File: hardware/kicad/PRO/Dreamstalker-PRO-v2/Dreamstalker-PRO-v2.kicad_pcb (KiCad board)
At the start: 2 copper layers, 79 x 85 mm, 110 parts, among them J1 UART Header, J2 JTAG Header, J3 ST-033, J4 ATTEND_112J-TDAR-R01, J5 USB Power, J6 Li-Po 3.7V, M1 Vibration Motor, Q1 IRLML2402, Q2 BC807-40, Q3 BC807-40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

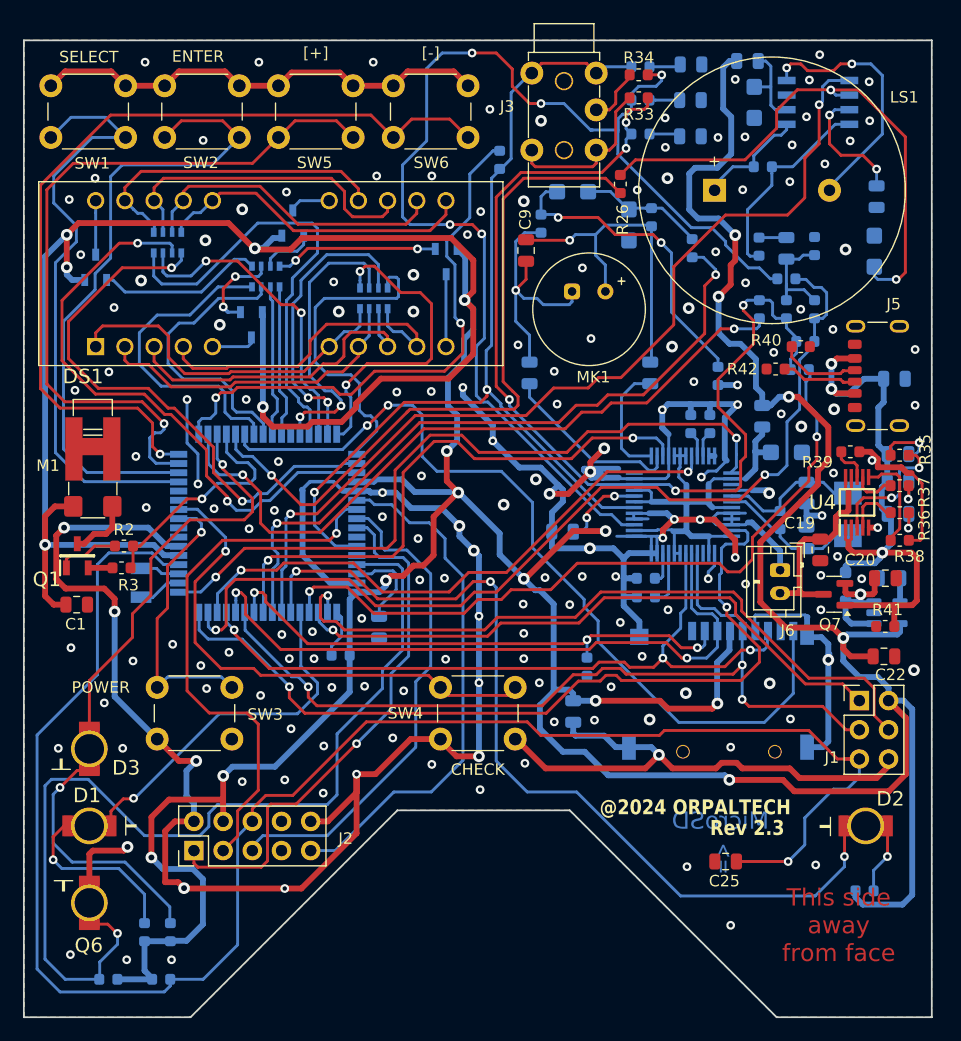
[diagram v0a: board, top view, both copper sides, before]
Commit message: 1) Fixed: battery monitor not able to detect low-battery state (Now get battery monitor signal from LDO input). 2) Other planned updates.
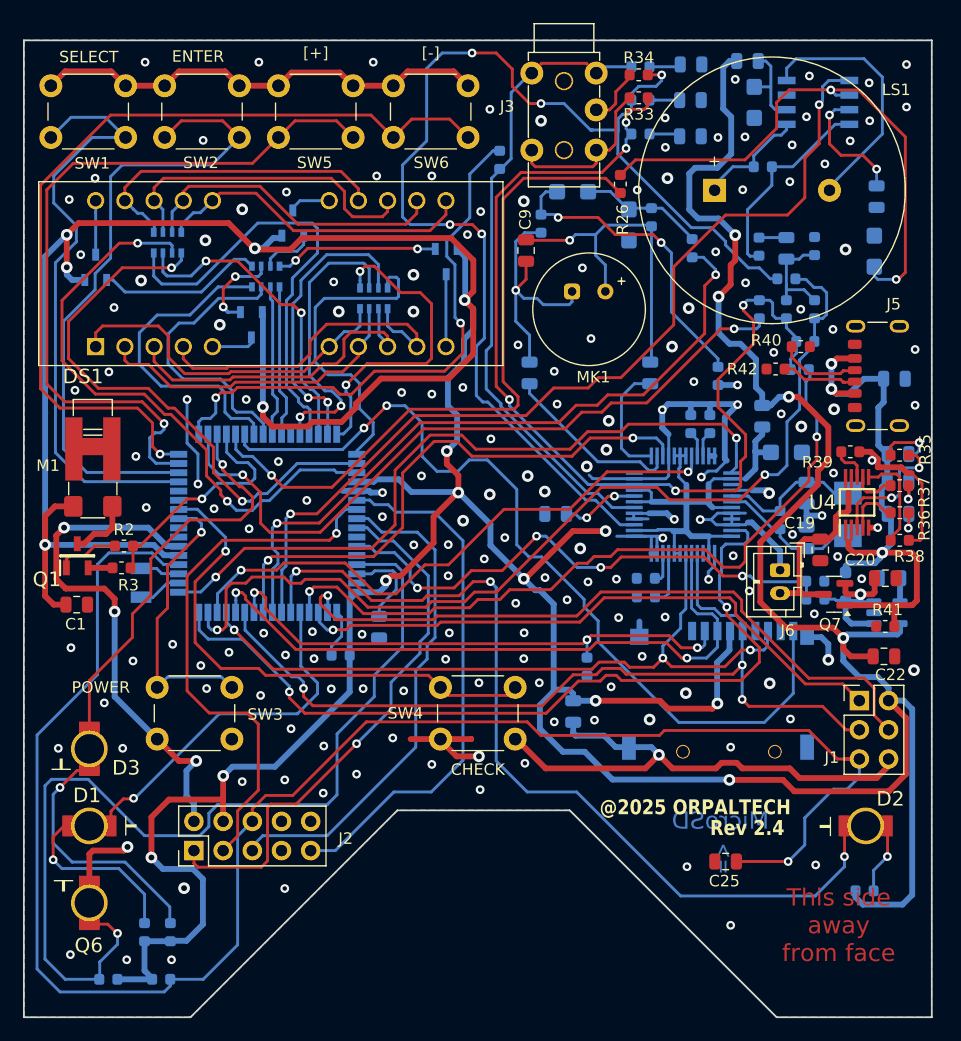
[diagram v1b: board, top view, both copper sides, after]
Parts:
- added R43: 30K, Dreamstalker-Footprints:R_0603_1608Metric, B.Cu at (158.4, 90.6)
- added R44: 15K, Dreamstalker-Footprints:R_0603_1608Metric, B.Cu at (158.4, 89.1)
- moved C13 1.65 mm to (135.8, 83.2)
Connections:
- U1 pad 59: /GBUF -> /BM
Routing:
- net GND: track 414.1 -> 250.1 mm, vias 174 -> 177
- net /BM: track 0.00 -> 47.1 mm, vias 0 -> 4
- net /GBUF: track 82.5 -> 56.1 mm, vias 2 -> 0
- net /VSVDD: track 43.2 -> 45.8 mm
- net /V_IN: track 12.0 -> 14.1 mm
- net /SILENT: track 61.8 -> 60.2 mm
- net /PDI: track 62.2 -> 60.8 mm
- net /XRESET: track 49.7 -> 48.5 mm
- net /XDCS: track 63.1 -> 62.1 mm
- net /TMS: track 42.9 -> 43.9 mm
- net /TCK: track 46.8 -> 47.7 mm
- net /TDI: track 45.5 -> 46.3 mm
- net /MOSI: track 57.7 -> 57.0 mm
- net /CD: track 74.4 -> 75.1 mm
- net +3V: track 456.5 -> 455.9 mm
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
